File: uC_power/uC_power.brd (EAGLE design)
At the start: 49.5 x 37.8 mm, 45 parts, among them SW1 TOGURUSUIITI

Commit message: Add files via upload
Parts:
- added C10: (no value), rcl:C1608
- added JP1, JP2: (no value), pinhead:1X02
- added R16: 10k, user_rcl:1608
- added R_I3: (no value), user_rcl:1005X4RESISTOR
- added TRIM_R3: 50k, user_rcl:PV23A
- R11, R8: value 20k -> 10k
- R13: value 10k -> 470k
- TRIM_R1, TRIM_R2: value 10k -> 22k
- U$9: value SSOT6_FET -> NJM2380; device user_tr_fet_igbt:SSOT6 -> user_ic:SOT23-5
- moved R13 7.57 mm to (29.2, 24.1), turned to 180 degrees
- moved U$9 4.39 mm to (25.5, 27.2), turned to 90 degrees
- moved R6 1.14 mm to (42.0, 25.4), turned to 180 degrees
- moved U$6 1.02 mm to (44.8, 37.3)
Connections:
- removed net N$17: R13.1, U$9.1, U$9.4
- removed net N$20: SW1.2, SW1.C, U$9.6
- new net N$19: C6.1, IC3.11, IC3.8, JP2.1, R6.1, TRIM_R2.1, U$2.4
- new net N$25: IC3.10, IC3.5, IC3.6, IC3.9, R_I3.5, R_I3.8
- new net V_SENS: C7.1, GYAKUSETU_FET.PIN1, GYAKUSETU_FET.PIN3, IC3.3, R10.2, R12.2, R5.2, R6.2, R7.1, R9.2, R_I1.5, R_I1.6, R_I1.7, R_I1.8, R_I3.1, SW_FET.PIN1, SW_FET.PIN3, TRIM_R3.1
- net COMP4: no longer U$9.3
- net GND: now also C10.2, JP1.2, JP2.2, R16.1, R_I3.4; no longer U$9.5
- net N$5: now also JP1.1
- net N$6: now also C10.1, SW1.2, SW1.C, U$9.4; no longer C6.1, IC3.11, IC3.8, R6.2, TRIM_R2.1, U$2.4
- net N$8: now also R13.1, R16.2, TRIM_R3.2, TRIM_R3.3, U$9.5; no longer C7.1, GYAKUSETU_FET.PIN1, GYAKUSETU_FET.PIN3, IC3.10, IC3.3, IC3.5, IC3.6, IC3.9, R10.2, R12.2, R13.2, R5.2, R6.1, R7.1, R9.2, R_I1.5, R_I1.6, R_I1.7, R_I1.8, SW_FET.PIN1, SW_FET.PIN3
- net V12: now also R13.2
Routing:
- net N$8: track 90.8 -> 9.38 mm, vias 6 -> 1
- net V_SENS: track 0.00 -> 72.3 mm, vias 0 -> 6
- net N$19: track 0.00 -> 21.5 mm, vias 0 -> 2
- net COMP4: track 25.9 -> 10.7 mm
- net N$5: track 16.1 -> 24.8 mm, vias 1 -> 2
- net N$25: track 0.00 -> 8.26 mm, vias 0 -> 2
- net N$20: track 6.09 -> 0.00 mm
- net N$17: track 5.85 -> 0.00 mm
- net N$6: track 17.2 -> 13.0 mm, vias 1 -> 0
- net V12: track 17.4 -> 21.2 mm, vias 2 -> 3
- net GND: track 41.5 -> 43.4 mm, vias 14 -> 13
- net N$14: track 1.74 -> 2.87 mm
- net N$12: track 2.41 -> 3.29 mm
- net N$13: track 1.47 -> 2.26 mm
- added copper zone on layer 1, net V_SENS
- removed copper zone on layer 1, net N$8
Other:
- board text added: "KRP"

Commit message: uvloを取っ払った
uvloを付けたのはいいけど調節がめんどくさいことに気が付いた
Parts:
- removed C10: (no value), rcl:C1608
- removed R13: 470k, user_rcl:1608
- removed R16: 10k, user_rcl:1608
- removed TRIM_R3: 50k, user_rcl:PV23A
- removed U$9: NJM2380, user_ic:SOT23-5
- moved GYAKUSETU_FET 1.27 mm to (25.4, 25.4)
- moved JP1 1.27 mm to (46.6, 25.0)
- moved JP2 1.27 mm to (46.6, 29.5)
- moved R10 1.27 mm to (35.9, 34.2)
- moved R5 1.27 mm to (39.8, 34.2)
- moved R9 1.27 mm to (32.1, 34.2)
- moved SW_FET 1.27 mm to (31.8, 25.4)
- moved U$3 1.27 mm to (33.4, 34.2)
- moved U$4 1.27 mm to (37.2, 34.2)
- moved U$5 1.27 mm to (41.0, 34.2)
- moved U$6 1.27 mm to (44.8, 36.1)
- moved IC1 1.27 mm to (12.7, 7.62)
- moved LED1 1.27 mm to (34.3, 7.62)
- moved R14 1.27 mm to (33.0, 7.62)
- moved R4 1.27 mm to (6.86, 5.84)
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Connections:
- removed net N$6: C10.1, SW1.2, SW1.C, U$9.4
- removed net N$8: R13.1, R16.2, TRIM_R3.2, TRIM_R3.3, U$9.5
- net GND: now also SW1.2, SW1.C; no longer C10.2, R16.1, U$9.2
- net V12: no longer R13.2
- net V_SENS: no longer TRIM_R3.1
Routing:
- net N$6: track 13.0 -> 0.00 mm
- net V_SENS: track 72.3 -> 62.1 mm, vias 6 -> 4
- net N$8: track 9.38 -> 0.00 mm, vias 1 -> 0
- net GND: track 43.4 -> 49.6 mm
- net V12: track 21.2 -> 17.4 mm, vias 3 -> 2
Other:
- board text added: "B_normal"
- board text added: "G_denger"
- board text added: "R_out of out"
- board text removed: "B正常"
- board text removed: "Gやばそう"
- board text removed: "Rダメ"

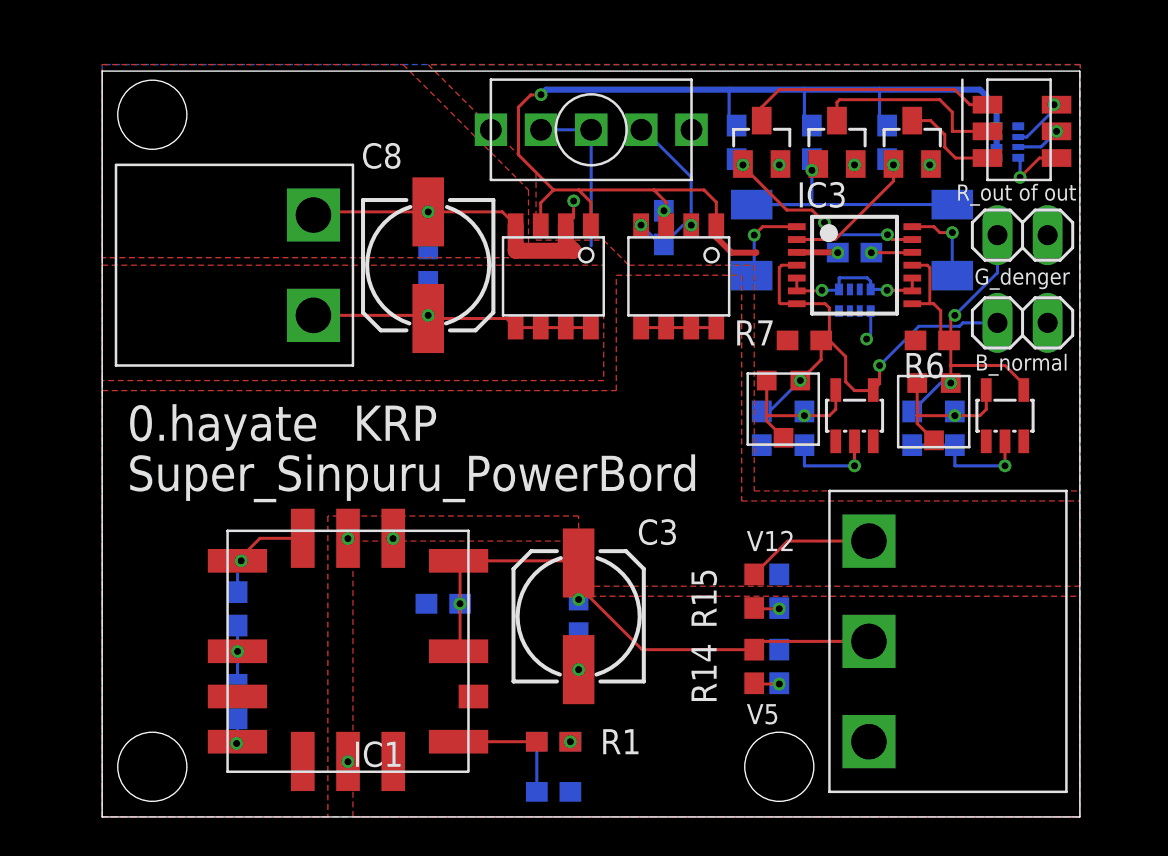
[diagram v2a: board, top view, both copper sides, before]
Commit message: UVLO、リセッタブルヒューズを追加
安全な自動シャットダウンのためのuvloを追加、ショート時の保護のためのリセッタブルヒューズを追加
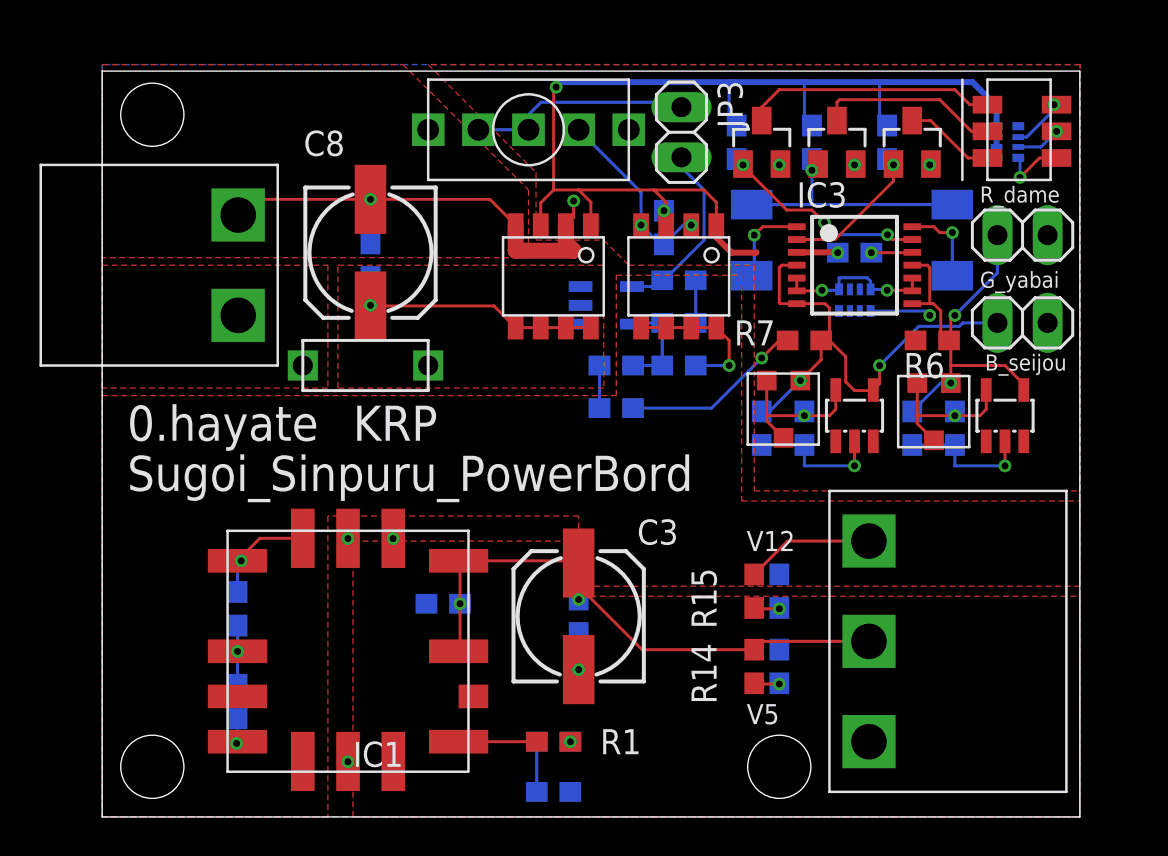
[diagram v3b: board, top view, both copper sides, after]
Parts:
- added C10: (no value), rcl:C1608
- added F1: (no value), user_hyuzu:RGEF300
- added JP3: (no value), pinhead:1X02
- added R13: 470k, user_rcl:1608
- added R16: 10k, user_rcl:1608
- added R17: 15k, user_rcl:1608
- added R18: 22k, user_rcl:1608
- added U$9: NJM2380, user_ic:SOT23-5
- moved U$11 3.81 mm to (8.89, 33.0)
- moved SW1 3.18 mm to (21.6, 34.8)
- moved C8 2.99 mm to (13.6, 28.6)
- moved C9 2.93 mm to (13.6, 28.2)
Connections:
- new net N$17: R17.1, R18.2
- new net N$20: JP3.1, SW1.2, SW1.C
- new net N$21: F1.P$2, U$11.P$1
- new net N$6: C10.1, JP3.2, U$9.4
- new net N$8: R13.1, R16.2, R18.1, U$9.5
- net GND: now also C10.2, R16.1, U$9.2; no longer SW1.2, SW1.C
- net V12: now also R13.2
- net VCC: now also F1.P$1; no longer U$11.P$1
- net V_SENS: now also R17.2
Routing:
- net N$20: track 0.00 -> 11.4 mm
- net V_SENS: track 62.1 -> 71.9 mm, vias 4 -> 5
- net N$6: track 0.00 -> 9.29 mm
- net N$8: track 0.00 -> 5.19 mm
- net V12: track 17.4 -> 21.2 mm, vias 2 -> 3
- net VCC: track 16.2 -> 13.3 mm
- net N$17: track 0.00 -> 2.16 mm
- net GND: track 49.6 -> 48.1 mm
- net N$10: track 9.84 -> 9.27 mm
- added copper zone on layer 1, net N$21
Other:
- board text added: "B_seijou"
- board text added: "G_yabai"
- board text added: "R_dame"
- board text added: "Sugoi_Sinpuru_PowerBord"
- board text removed: "B_normal"
- board text removed: "G_denger"
- board text removed: "R_out of out"
- board text removed: "Super_Sinpuru_PowerBord"
